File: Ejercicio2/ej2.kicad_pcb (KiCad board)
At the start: 2 copper layers, 40.6 x 61 mm, 8 parts, among them J301 DB9-F, U301 SP3232ECN

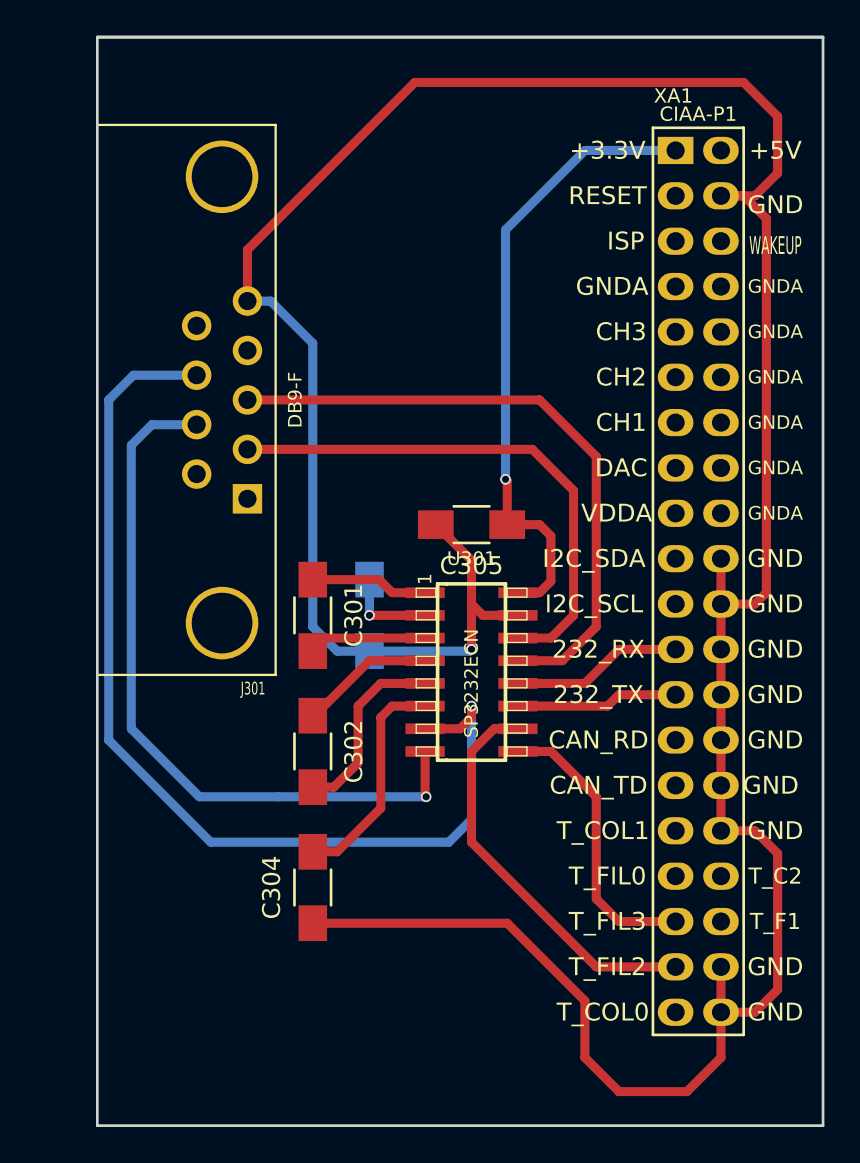
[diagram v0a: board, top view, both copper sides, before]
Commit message: Ajustes en las referencias del pcb para reflejar cambios en el esquemático.
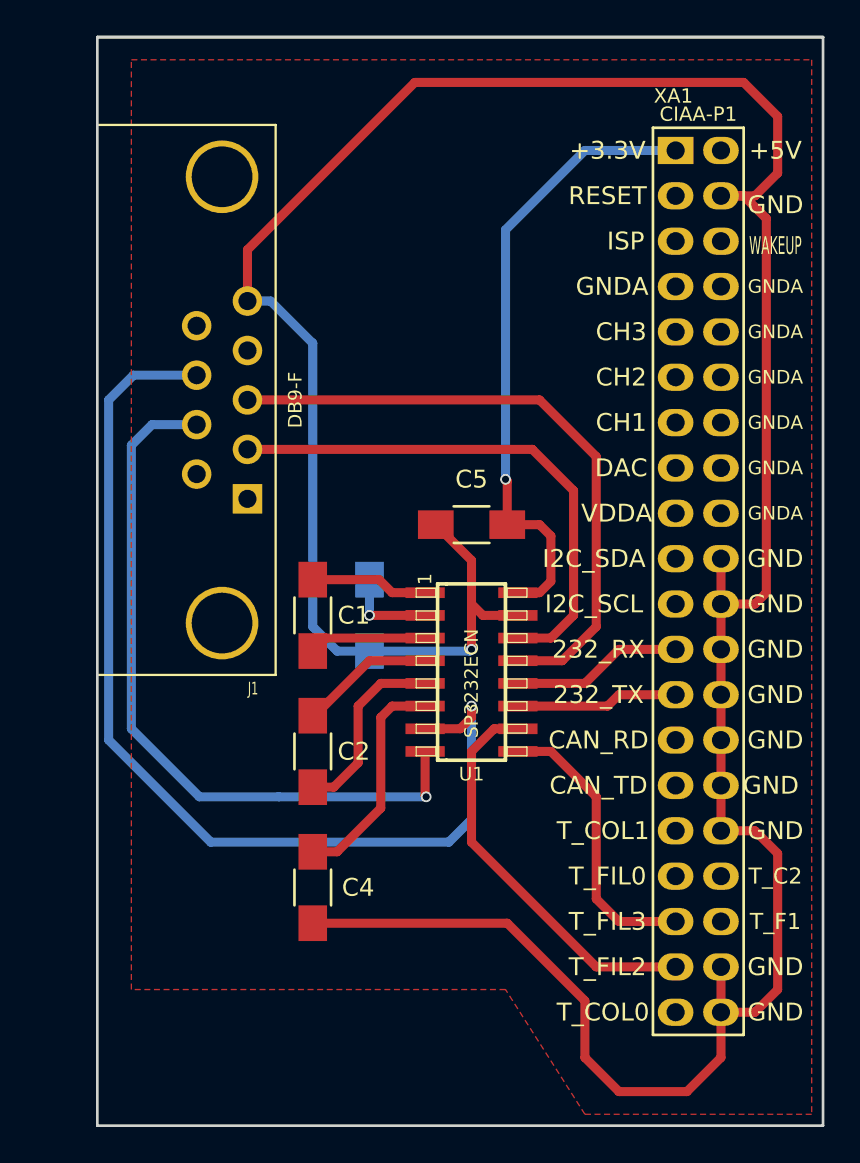
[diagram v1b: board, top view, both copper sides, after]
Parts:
- renumbered C301 to C1, C302 to C2, C303 to C3, C304 to C4, C305 to C5, J301 to J1, U301 to U1
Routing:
- added copper zone on F.Cu, net GND
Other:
- net class Default: clearance 0.2 -> 0.508
- rule trace_clearance: 0.2 -> 0.508

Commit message: Agregado de zonas de cobre (Igual hay que rehacer con plano de tierra).
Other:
- board text added: "INDUSTRIA ARGENTINA"
- board text added: "INTI - CMNB"
- board text added: "Instituto Nacional de Tecnología Industrial"
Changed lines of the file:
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@@
     (area 102.159999 73.584999 142.950001 134.695001)
     (thickness 1.6)
-    (drawings 5)
+    (drawings 10)
     (tracks 125)
     (zones 0)
@@
     (user_trace_width 0.508)
     (trace_clearance 0.508)
-    (zone_clearance 0.808)
+    (zone_clearance 0.508)
     (zone_45_only no)
     (trace_min 0.2)
@@
     (pad 30 thru_hole oval (at 2.54 35.56 270) (size 1.524 2) (drill 1.016) (layers *.Cu *.Mask F.SilkS)
       (net 1 GND))
+  )
+  (dimension 40.64 (width 0.3) (layer Dwgs.User)
+    (gr_text 40,640mm (at 122.555 67.23) (layer Dwgs.User)
+      (effects (font (size 1.5 1.5) (thickness 0.3)))
+    )
+    (feature1 (pts (xy 142.875 73.66) (xy 142.875 65.88)))
+    (feature2 (pts (xy 102.235 73.66) (xy 102.235 65.88)))
+    (crossbar (pts (xy 102.235 68.58) (xy 142.875 68.58)))
+    (arrow1a (pts (xy 142.875 68.58) (xy 141.748496 69.166421)))
+    (arrow1b (pts (xy 142.875 68.58) (xy 141.748496 67.993579)))
+    (arrow2a (pts (xy 102.235 68.58) (xy 103.361504 69.166421)))
+    (arrow2b (pts (xy 102.235 68.58) (xy 103.361504 67.993579)))
+  )
+  (dimension 60.96 (width 0.3) (layer Dwgs.User)
+    (gr_text 60,960mm (at 151.845 104.14 270) (layer Dwgs.User)
+      (effects (font (size 1.5 1.5) (thickness 0.3)))
+    )
+    (feature1 (pts (xy 142.875 134.62) (xy 153.195 134.62)))
+    (feature2 (pts (xy 142.875 73.66) (xy 153.195 73.66)))
+    (crossbar (pts (xy 150.495 73.66) (xy 150.495 134.62)))
+    (arrow1a (pts (xy 150.495 134.62) (xy 149.908579 133.493496)))
+    (arrow1b (pts (xy 150.495 134.62) (xy 151.081421 133.493496)))
+    (arrow2a (pts (xy 150.495 73.66) (xy 149.908579 74.786504)))
+    (arrow2b (pts (xy 150.495 73.66) (xy 151.081421 74.786504)))
+  )
+  (gr_text "Instituto Nacional de Tecnología Industrial" (at 120.015 132.715) (layer F.SilkS)
+    (effects (font (size 1.5 1) (thickness 0.25)))
+  )
+  (gr_text "INDUSTRIA ARGENTINA" (at 115.57 127.635) (layer B.Cu)
+    (effects (font (size 1.5 1.5) (thickness 0.3)) (justify mirror))
+  )
+  (gr_text "INTI - CMNB" (at 110.49 130.175) (layer F.Cu)
+    (effects (font (size 1.5 1.5) (thickness 0.3)))
   )
   (gr_line (start 102.235 73.66) (end 142.875 73.66) (angle 90) (layer Edge.Cuts) (width 0.15))
@@
     (polygon
       (pts
-        (xy 104.14 74.93) (xy 142.24 74.93) (xy 142.24 133.985) (xy 129.54 133.985) (xy 125.095 127)
-        (xy 104.14 127)
+        (xy 142.24 133.35) (xy 129.54 133.35) (xy 124.46 126.365) (xy 102.87 126.365) (xy 102.87 75.565)
+        (xy 142.24 75.565) (xy 142.24 133.35)
       )
     )
+  )
+  (zone (net 0) (net_name "") (layer F.Cu) (hatch edge 0.508)
+    (connect_pads (clearance 0.508))
+    (min_thickness 0.254)
+    (keepout (tracks allowed) (vias allowed) (copperpour not_allowed))
+    (fill (arc_segments 16) (thermal_gap 0.508) (thermal_bridge_width 0.508))
+    (polygon
+      (pts
+        (xy 127.635 115.57) (xy 118.11 115.57) (xy 118.11 102.235) (xy 127.635 102.235) (xy 127.635 115.57)
+      )
+    )

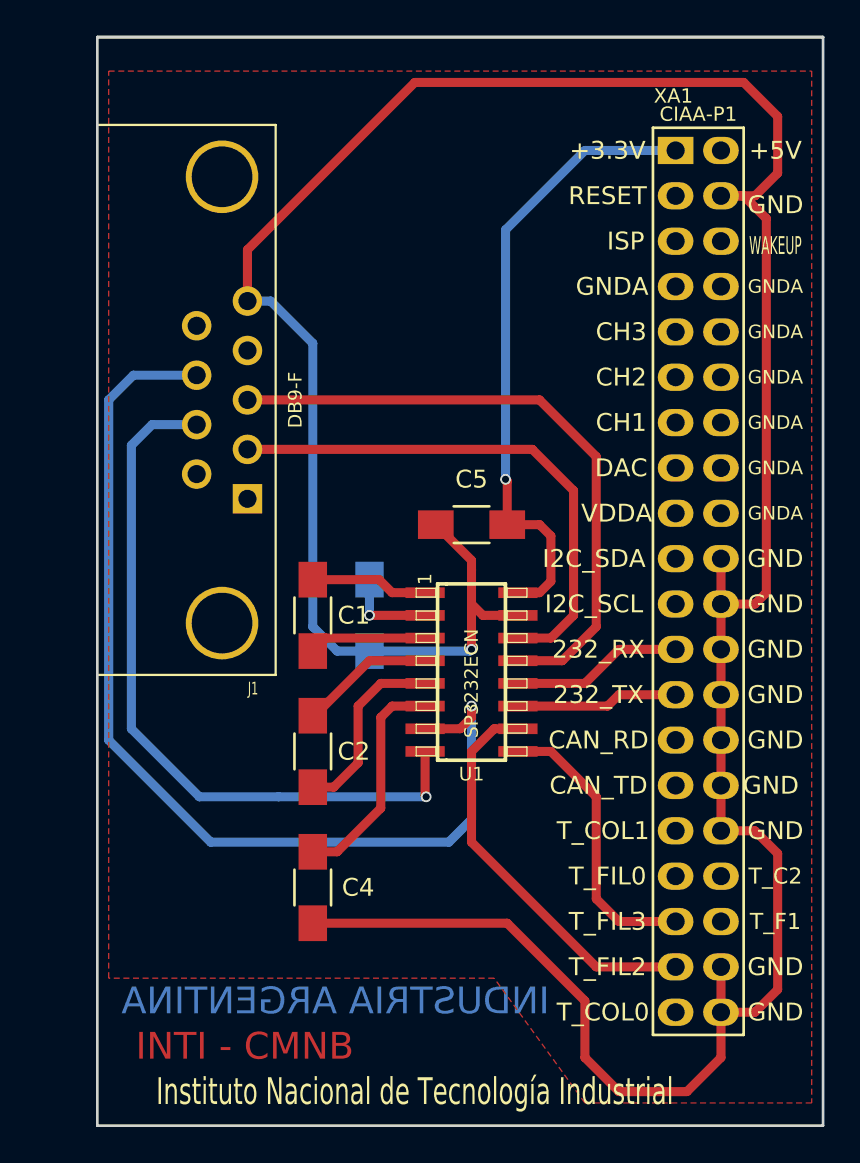
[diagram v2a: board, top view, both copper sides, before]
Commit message: Versión del Ejercicio2 con CAN.
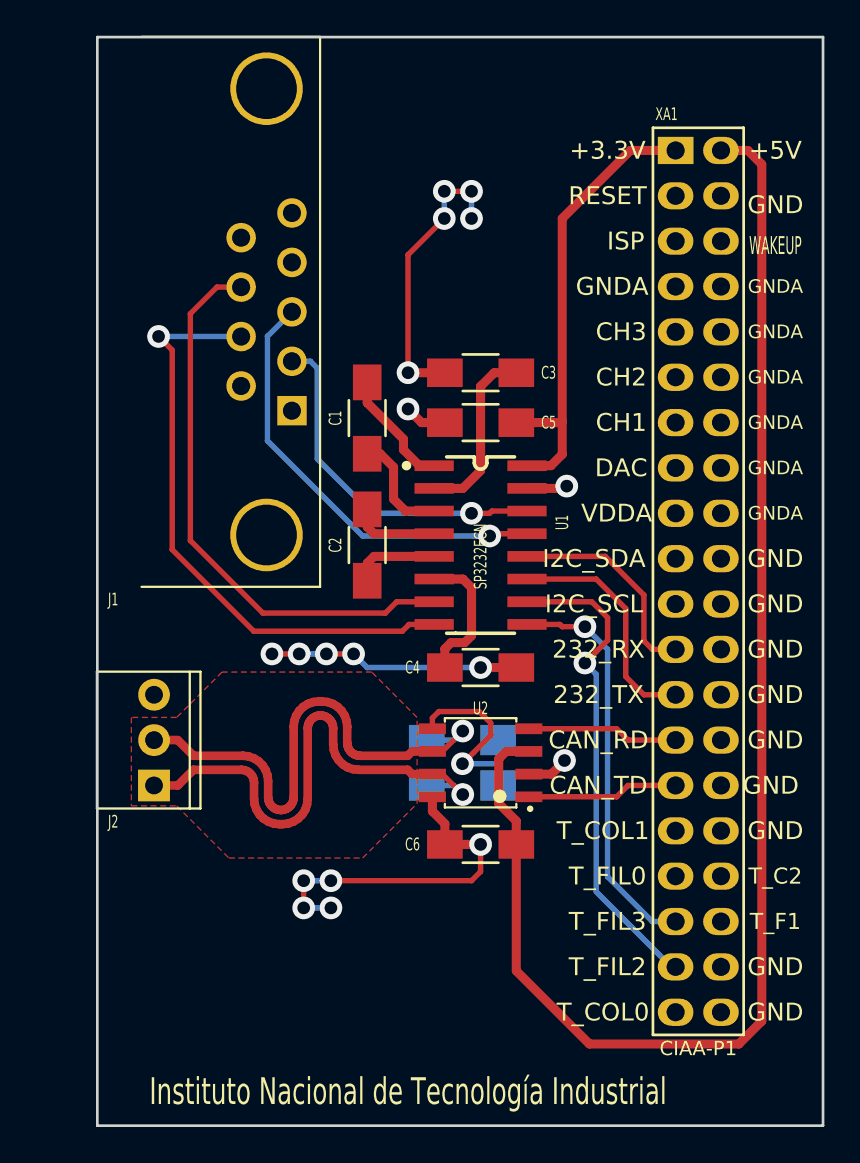
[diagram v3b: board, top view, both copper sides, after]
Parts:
- added C6: 100nF, Capacitors_SMD:C_1206_HandSoldering, F.Cu at (123.7, 118.9)
- added J2: CAN, ej2:CON_PALETA_3, F.Cu at (105.4, 113.0)
- added R1: 60, Resistors_SMD:R_1206_HandSoldering, B.Cu at (122.7, 115.6)
- added R2: 60, Resistors_SMD:R_1206_HandSoldering, B.Cu at (122.7, 113.0)
- added U2: AMIS42665TJAA1RG, ej2:SOIC-8, F.Cu at (123.7, 114.3)
- C3: moved to F.Cu
- moved C4 15.5 mm to (123.7, 109.0), turned to 180 degrees
- moved C3 14.9 mm to (123.7, 92.5), turned to 0 degrees
- moved C2 12.0 mm to (117.3, 102.1)
- moved C1 11.5 mm to (117.3, 95.0)
- moved U1 7.13 mm to (123.7, 102.1)
- moved C5 5.74 mm to (123.7, 95.2)
- moved J1 5.53 mm to (111.7, 89.0)
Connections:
- XA1 pad 2: (no net) -> +5V
- XA1 pad 27: (no net) -> /Conector/CAN_RX
- XA1 pad 29: (no net) -> /Conector/CAN_TX
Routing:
- net GND: track 176.4 -> 56.8 mm, vias 1 -> 18
- net +5V: track 0.00 -> 80.7 mm
- net /Conector/CAN_P: track 0.00 -> 29.9 mm, vias 0 -> 1
- net /Conector/CAN_N: track 0.00 -> 29.9 mm, vias 0 -> 1
- net Net-(J1-Pad8): track 57.6 -> 31.8 mm, vias 1 -> 0
- net Net-(R1-Pad2): track 0.00 -> 11.8 mm, vias 0 -> 1
- net Net-(J1-Pad3): track 35.5 -> 24.6 mm, vias 0 -> 1
- net Net-(J1-Pad2): track 29.8 -> 19.7 mm, vias 0 -> 1
- net +3.3V: track 35.8 -> 26.0 mm, vias 1 -> 0
- net /Conector/CAN_TX: track 0.00 -> 8.49 mm
- net /Conector/CAN_RX: track 0.00 -> 8.49 mm
- net Net-(J1-Pad7): track 40.7 -> 33.6 mm
- net /Conector/RTS: track 16.1 -> 22.7 mm, vias 0 -> 1
- net Net-(C2-Pad2): track 10.6 -> 4.89 mm
- net Net-(C3-Pad2): track 5.12 -> 10.0 mm, vias 1 -> 0
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- added copper zone on B.Cu, net GND
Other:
- net class Default: clearance 0.508 -> 0.2794; trace_width 0.25 -> 0.3048; via_dia 0.6 -> 1.27; via_drill 0.4 -> 0.7112
- rule trace_clearance: 0.508 -> 0.2794
- rule trace_min: 0.2 -> 0.2794
- rule via_min_drill: 0.3 -> 0.7112
- rule via_min_size: 0.4 -> 1.27
